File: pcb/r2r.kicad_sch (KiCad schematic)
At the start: 8 parts

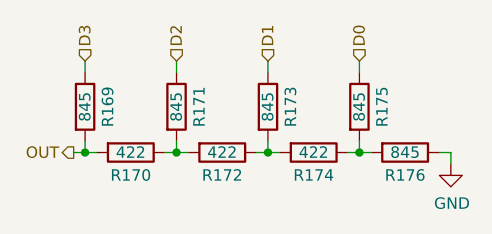
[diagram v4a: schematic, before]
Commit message: WIP PCB (add bypass caps, minor fixes)
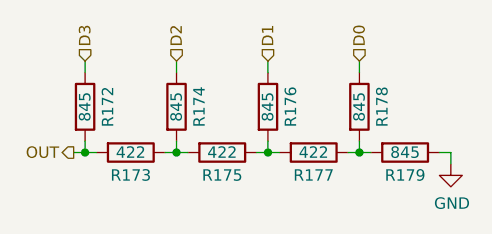
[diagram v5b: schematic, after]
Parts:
- renumbered R169 to R172, R170 to R173, R171 to R174, R172 to R175, R173 to R176, R174 to R177, R175 to R178, R176 to R179
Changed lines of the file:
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@@
 		(on_board yes)
 		(dnp no)
-		(property "Reference" "#PWR0492"
+		(property "Reference" "#PWR0547"
 			(at 96.52 50.8 0)
 			(effects
@@
 			(project "fnx51"
 				(path "/e63e39d7-6ac0-4ffd-8aa3-1841a4541b55/90e1f016-3c60-4383-aa8d-def9977ac47b/91068912-38bb-46cd-9b18-d1871085dfd0"
-					(reference "#PWR0494")
-					(unit 1)
-				)
-				(path "/e63e39d7-6ac0-4ffd-8aa3-1841a4541b55/90e1f016-3c60-4383-aa8d-def9977ac47b/aa0b7daf-7acd-446b-bc05-f74af189bf7c"
-					(reference "#PWR0493")
-					(unit 1)
-				)
-				(path "/e63e39d7-6ac0-4ffd-8aa3-1841a4541b55/90e1f016-3c60-4383-aa8d-def9977ac47b/dde75323-f81a-495f-a05e-373a126dd215"
-					(reference "#PWR0492")
+					(reference "#PWR0549")
+					(unit 1)
+				)
+				(path "/e63e39d7-6ac0-4ffd-8aa3-1841a4541b55/90e1f016-3c60-4383-aa8d-def9977ac47b/aa0b7daf-7acd-446b-bc05-f74af189bf7c"
+					(reference "#PWR0548")
+					(unit 1)
+				)
+				(path "/e63e39d7-6ac0-4ffd-8aa3-1841a4541b55/90e1f016-3c60-4383-aa8d-def9977ac47b/dde75323-f81a-495f-a05e-373a126dd215"
+					(reference "#PWR0547")
 					(unit 1)
 				)
@@
 		(on_board yes)
 		(dnp no)
-		(property "Reference" "R175"
+		(property "Reference" "R178"
 			(at 88.9 38.1 90)
 			(effects
@@
 			(project "fnx51"
 				(path "/e63e39d7-6ac0-4ffd-8aa3-1841a4541b55/90e1f016-3c60-4383-aa8d-def9977ac47b/91068912-38bb-46cd-9b18-d1871085dfd0"
-					(reference "R191")
-					(unit 1)
-				)
-				(path "/e63e39d7-6ac0-4ffd-8aa3-1841a4541b55/90e1f016-3c60-4383-aa8d-def9977ac47b/aa0b7daf-7acd-446b-bc05-f74af189bf7c"
-					(reference "R183")
-					(unit 1)
-				)
-				(path "/e63e39d7-6ac0-4ffd-8aa3-1841a4541b55/90e1f016-3c60-4383-aa8d-def9977ac47b/dde75323-f81a-495f-a05e-373a126dd215"
-					(reference "R175")
+					(reference "R194")
+					(unit 1)
+				)
+				(path "/e63e39d7-6ac0-4ffd-8aa3-1841a4541b55/90e1f016-3c60-4383-aa8d-def9977ac47b/aa0b7daf-7acd-446b-bc05-f74af189bf7c"
+					(reference "R186")
+					(unit 1)
+				)
+				(path "/e63e39d7-6ac0-4ffd-8aa3-1841a4541b55/90e1f016-3c60-4383-aa8d-def9977ac47b/dde75323-f81a-495f-a05e-373a126dd215"
+					(reference "R178")
 					(unit 1)
 				)
@@
 		(on_board yes)
 		(dnp no)
-		(property "Reference" "R171"
+		(property "Reference" "R174"
 			(at 68.58 38.1 90)
 			(effects
@@
 			(project "fnx51"
 				(path "/e63e39d7-6ac0-4ffd-8aa3-1841a4541b55/90e1f016-3c60-4383-aa8d-def9977ac47b/91068912-38bb-46cd-9b18-d1871085dfd0"
-					(reference "R187")
-					(unit 1)
-				)
-				(path "/e63e39d7-6ac0-4ffd-8aa3-1841a4541b55/90e1f016-3c60-4383-aa8d-def9977ac47b/aa0b7daf-7acd-446b-bc05-f74af189bf7c"
-					(reference "R179")
-					(unit 1)
-				)
-				(path "/e63e39d7-6ac0-4ffd-8aa3-1841a4541b55/90e1f016-3c60-4383-aa8d-def9977ac47b/dde75323-f81a-495f-a05e-373a126dd215"
-					(reference "R171")
+					(reference "R190")
+					(unit 1)
+				)
+				(path "/e63e39d7-6ac0-4ffd-8aa3-1841a4541b55/90e1f016-3c60-4383-aa8d-def9977ac47b/aa0b7daf-7acd-446b-bc05-f74af189bf7c"
+					(reference "R182")
+					(unit 1)
+				)
+				(path "/e63e39d7-6ac0-4ffd-8aa3-1841a4541b55/90e1f016-3c60-4383-aa8d-def9977ac47b/dde75323-f81a-495f-a05e-373a126dd215"
+					(reference "R174")
 					(unit 1)
 				)
@@
 		(on_board yes)
 		(dnp no)
-		(property "Reference" "R172"
+		(property "Reference" "R175"
 			(at 71.12 45.72 90)
 			(effects
@@
 			(project "fnx51"
 				(path "/e63e39d7-6ac0-4ffd-8aa3-1841a4541b55/90e1f016-3c60-4383-aa8d-def9977ac47b/91068912-38bb-46cd-9b18-d1871085dfd0"
-					(reference "R188")
-					(unit 1)
-				)
-				(path "/e63e39d7-6ac0-4ffd-8aa3-1841a4541b55/90e1f016-3c60-4383-aa8d-def9977ac47b/aa0b7daf-7acd-446b-bc05-f74af189bf7c"
-					(reference "R180")
-					(unit 1)
-				)
-				(path "/e63e39d7-6ac0-4ffd-8aa3-1841a4541b55/90e1f016-3c60-4383-aa8d-def9977ac47b/dde75323-f81a-495f-a05e-373a126dd215"
-					(reference "R172")
+					(reference "R191")
+					(unit 1)
+				)
+				(path "/e63e39d7-6ac0-4ffd-8aa3-1841a4541b55/90e1f016-3c60-4383-aa8d-def9977ac47b/aa0b7daf-7acd-446b-bc05-f74af189bf7c"
+					(reference "R183")
+					(unit 1)
+				)
+				(path "/e63e39d7-6ac0-4ffd-8aa3-1841a4541b55/90e1f016-3c60-4383-aa8d-def9977ac47b/dde75323-f81a-495f-a05e-373a126dd215"
+					(reference "R175")
 					(unit 1)
 				)
@@
 		(on_board yes)
 		(dnp no)
-		(property "Reference" "R173"
+		(property "Reference" "R176"
 			(at 78.74 38.1 90)
 			(effects
@@
 			(project "fnx51"
 				(path "/e63e39d7-6ac0-4ffd-8aa3-1841a4541b55/90e1f016-3c60-4383-aa8d-def9977ac47b/91068912-38bb-46cd-9b18-d1871085dfd0"
-					(reference "R189")
-					(unit 1)
-				)
-				(path "/e63e39d7-6ac0-4ffd-8aa3-1841a4541b55/90e1f016-3c60-4383-aa8d-def9977ac47b/aa0b7daf-7acd-446b-bc05-f74af189bf7c"
-					(reference "R181")
-					(unit 1)
-				)
-				(path "/e63e39d7-6ac0-4ffd-8aa3-1841a4541b55/90e1f016-3c60-4383-aa8d-def9977ac47b/dde75323-f81a-495f-a05e-373a126dd215"
-					(reference "R173")
+					(reference "R192")
+					(unit 1)
+				)
+				(path "/e63e39d7-6ac0-4ffd-8aa3-1841a4541b55/90e1f016-3c60-4383-aa8d-def9977ac47b/aa0b7daf-7acd-446b-bc05-f74af189bf7c"
+					(reference "R184")
+					(unit 1)
+				)
+				(path "/e63e39d7-6ac0-4ffd-8aa3-1841a4541b55/90e1f016-3c60-4383-aa8d-def9977ac47b/dde75323-f81a-495f-a05e-373a126dd215"
+					(reference "R176")
 					(unit 1)
 				)
@@
 		(on_board yes)
 		(dnp no)
-		(property "Reference" "R176"
+		(property "Reference" "R179"
 			(at 91.44 45.72 90)
 			(effects
@@
 			(project "fnx51"
 				(path "/e63e39d7-6ac0-4ffd-8aa3-1841a4541b55/90e1f016-3c60-4383-aa8d-def9977ac47b/91068912-38bb-46cd-9b18-d1871085dfd0"
-					(reference "R192")
-					(unit 1)
-				)
-				(path "/e63e39d7-6ac0-4ffd-8aa3-1841a4541b55/90e1f016-3c60-4383-aa8d-def9977ac47b/aa0b7daf-7acd-446b-bc05-f74af189bf7c"
-					(reference "R184")
-					(unit 1)
-				)
-				(path "/e63e39d7-6ac0-4ffd-8aa3-1841a4541b55/90e1f016-3c60-4383-aa8d-def9977ac47b/dde75323-f81a-495f-a05e-373a126dd215"
-					(reference "R176")
+					(reference "R195")
+					(unit 1)
+				)
+				(path "/e63e39d7-6ac0-4ffd-8aa3-1841a4541b55/90e1f016-3c60-4383-aa8d-def9977ac47b/aa0b7daf-7acd-446b-bc05-f74af189bf7c"
+					(reference "R187")
+					(unit 1)
+				)
+				(path "/e63e39d7-6ac0-4ffd-8aa3-1841a4541b55/90e1f016-3c60-4383-aa8d-def9977ac47b/dde75323-f81a-495f-a05e-373a126dd215"
+					(reference "R179")
 					(unit 1)
 				)
@@
 		(on_board yes)
 		(dnp no)
-		(property "Reference" "R170"
+		(property "Reference" "R173"
 			(at 60.96 45.72 90)
 			(effects
@@
 			(project "fnx51"
 				(path "/e63e39d7-6ac0-4ffd-8aa3-1841a4541b55/90e1f016-3c60-4383-aa8d-def9977ac47b/91068912-38bb-46cd-9b18-d1871085dfd0"
-					(reference "R186")
-					(unit 1)
-				)
-				(path "/e63e39d7-6ac0-4ffd-8aa3-1841a4541b55/90e1f016-3c60-4383-aa8d-def9977ac47b/aa0b7daf-7acd-446b-bc05-f74af189bf7c"
-					(reference "R178")
-					(unit 1)
-				)
-				(path "/e63e39d7-6ac0-4ffd-8aa3-1841a4541b55/90e1f016-3c60-4383-aa8d-def9977ac47b/dde75323-f81a-495f-a05e-373a126dd215"
-					(reference "R170")
+					(reference "R189")
+					(unit 1)
+				)
+				(path "/e63e39d7-6ac0-4ffd-8aa3-1841a4541b55/90e1f016-3c60-4383-aa8d-def9977ac47b/aa0b7daf-7acd-446b-bc05-f74af189bf7c"
+					(reference "R181")
+					(unit 1)
+				)
+				(path "/e63e39d7-6ac0-4ffd-8aa3-1841a4541b55/90e1f016-3c60-4383-aa8d-def9977ac47b/dde75323-f81a-495f-a05e-373a126dd215"
+					(reference "R173")
 					(unit 1)
 				)
@@
 		(on_board yes)
 		(dnp no)
-		(property "Reference" "R174"
+		(property "Reference" "R177"
 			(at 81.28 45.72 90)
 			(effects
@@
 			(project "fnx51"
 				(path "/e63e39d7-6ac0-4ffd-8aa3-1841a4541b55/90e1f016-3c60-4383-aa8d-def9977ac47b/91068912-38bb-46cd-9b18-d1871085dfd0"
-					(reference "R190")
-					(unit 1)
-				)
-				(path "/e63e39d7-6ac0-4ffd-8aa3-1841a4541b55/90e1f016-3c60-4383-aa8d-def9977ac47b/aa0b7daf-7acd-446b-bc05-f74af189bf7c"
-					(reference "R182")
-					(unit 1)
-				)
-				(path "/e63e39d7-6ac0-4ffd-8aa3-1841a4541b55/90e1f016-3c60-4383-aa8d-def9977ac47b/dde75323-f81a-495f-a05e-373a126dd215"
-					(reference "R174")
+					(reference "R193")
+					(unit 1)
+				)
+				(path "/e63e39d7-6ac0-4ffd-8aa3-1841a4541b55/90e1f016-3c60-4383-aa8d-def9977ac47b/aa0b7daf-7acd-446b-bc05-f74af189bf7c"
+					(reference "R185")
+					(unit 1)
+				)
+				(path "/e63e39d7-6ac0-4ffd-8aa3-1841a4541b55/90e1f016-3c60-4383-aa8d-def9977ac47b/dde75323-f81a-495f-a05e-373a126dd215"
+					(reference "R177")
 					(unit 1)
 				)
@@
 		(on_board yes)
 		(dnp no)
-		(property "Reference" "R169"
+		(property "Reference" "R172"
 			(at 58.42 38.1 90)
 			(effects
@@
 			(project "fnx51"
 				(path "/e63e39d7-6ac0-4ffd-8aa3-1841a4541b55/90e1f016-3c60-4383-aa8d-def9977ac47b/91068912-38bb-46cd-9b18-d1871085dfd0"
-					(reference "R185")
-					(unit 1)
-				)
-				(path "/e63e39d7-6ac0-4ffd-8aa3-1841a4541b55/90e1f016-3c60-4383-aa8d-def9977ac47b/aa0b7daf-7acd-446b-bc05-f74af189bf7c"
-					(reference "R177")
-					(unit 1)
-				)
-				(path "/e63e39d7-6ac0-4ffd-8aa3-1841a4541b55/90e1f016-3c60-4383-aa8d-def9977ac47b/dde75323-f81a-495f-a05e-373a126dd215"
-					(reference "R169")
-					(unit 1)
-				)
+					(reference "R188")
+					(unit 1)
+				)
+				(path "/e63e39d7-6ac0-4ffd-8aa3-1841a4541b55/90e1f016-3c60-4383-aa8d-def9977ac47b/aa0b7daf-7acd-446b-bc05-f74af189bf7c"
+					(reference "R180")
+					(unit 1)
+				)
+				(path "/e63e39d7-6ac0-4ffd-8aa3-1841a4541b55/90e1f016-3c60-4383-aa8d-def9977ac47b/dde75323-f81a-495f-a05e-373a126dd215"
+					(reference "R172")
+					(unit 1)
+				)
